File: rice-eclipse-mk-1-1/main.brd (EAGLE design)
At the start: 110.2 x 91.2 mm, 75 parts, among them IC1 LMV321LICTRT, IC2 LMV321LICTRT, IC3 LMV321LICTRT, IC4 LMV321LICTRT, U1 LM1084ISX-5.0/NOPB, U2 THS4531IDRD8-M, U3 THS4531IDRD8-M, U4 THS4531IDRD8-M, U5 THS4531IDRD8-M, U6 1101M2S3CQE2, X1 2540-5

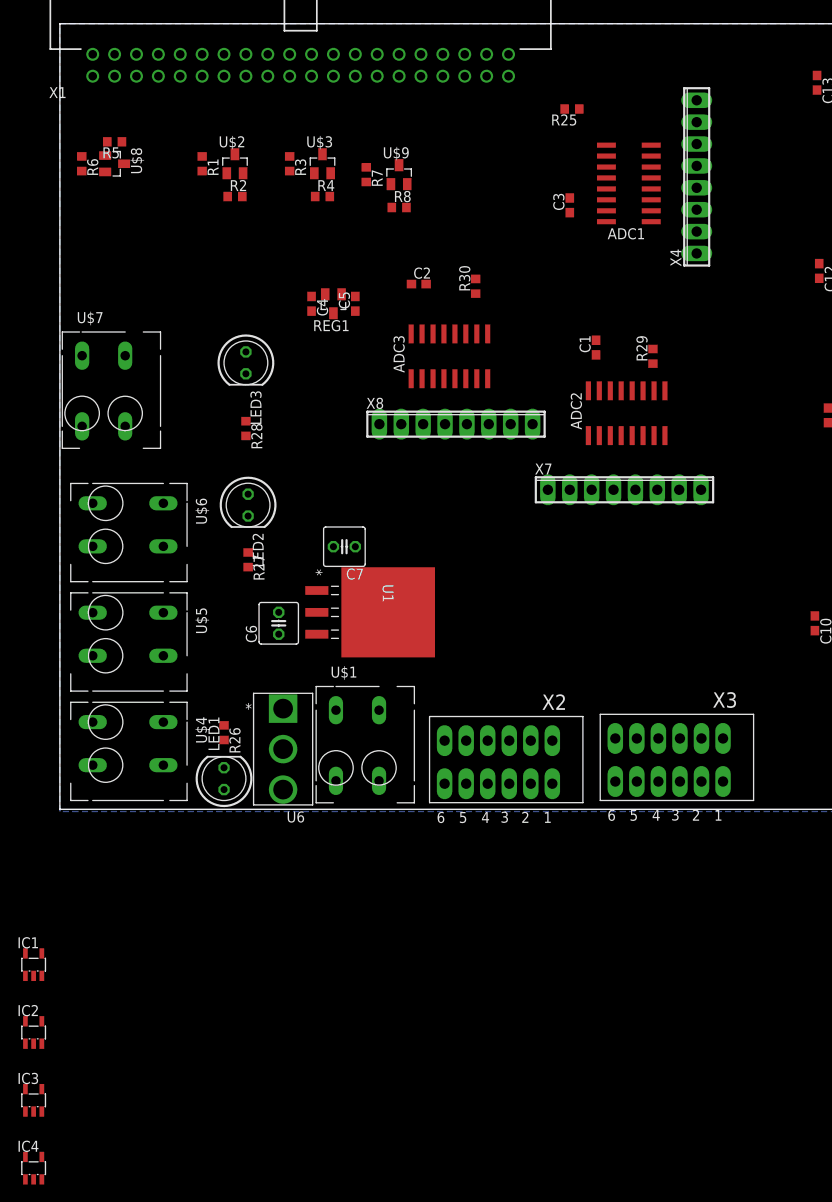
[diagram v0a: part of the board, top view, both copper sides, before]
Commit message: Added initial PT circuit guess and
added some routes for power.
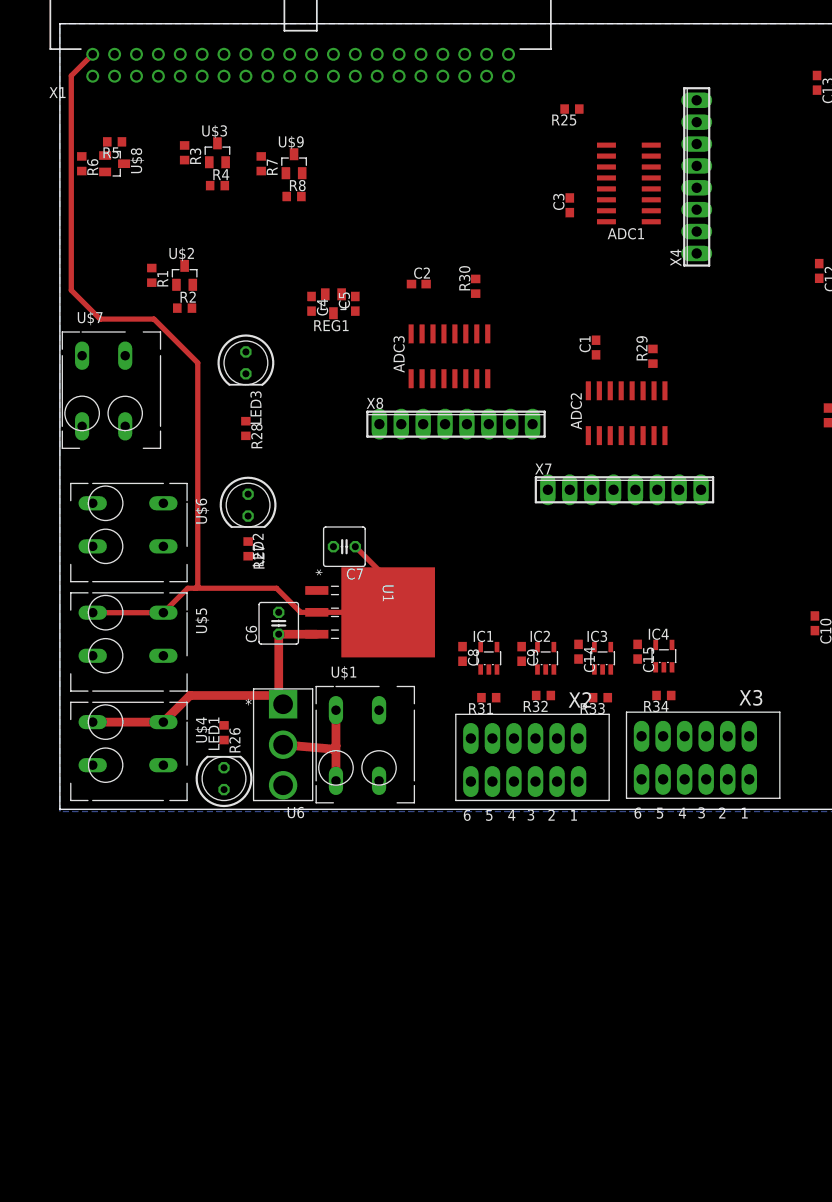
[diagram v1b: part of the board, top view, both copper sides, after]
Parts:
- added C14, C15, C8, C9: 10nF, rcl:C0603
- added R31, R32, R33, R34: 150, rcl:R0603
- moved IC4 94.3 mm to (70.1, 17.8)
- moved IC3 83.6 mm to (63.0, 17.5)
- moved IC2 73.6 mm to (56.4, 17.5)
- moved IC1 63.7 mm to (49.8, 17.5)
- moved R1 14.2 mm to (10.7, 62.0)
- moved R2 14.2 mm to (14.5, 58.2)
- moved U$2 14.2 mm to (14.5, 62.0)
- moved R7 12.3 mm to (23.4, 74.9)
- moved R3 12.3 mm to (14.5, 76.2)
- moved R4 12.3 mm to (18.3, 72.4)
- moved U$3 12.3 mm to (18.3, 76.2)
- moved R8 12.3 mm to (27.2, 71.1)
- moved U$9 12.3 mm to (27.2, 74.9)
- moved X3 3.06 mm to (83.6, 11.2)
- moved X2 3.06 mm to (63.8, 10.9)
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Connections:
- new net PT1_VS-: IC1.1, R31.2, X2.P$11, X2.P$5
- new net PT2_VS-: IC2.1, R32.2, X2.P$3, X2.P$9
- new net PT3_VS-: IC3.1, R33.2, X2.P$1, X2.P$7
- new net PT4_VS-: IC4.1, R34.2, X3.P$11, X3.P$5
- net +12V: now also X2.P$10, X2.P$12, X2.P$2, X2.P$4, X2.P$6, X2.P$8, X3.P$12, X3.P$6
- net +3V3: now also C14.1, C15.1, C8.1, C9.1, IC1.5, IC2.5, IC3.5, IC4.5
- net ADC2_A0: now also IC1.3, IC1.4; no longer X2.P$12, X2.P$6
- net ADC2_A1: now also IC2.3, IC2.4; no longer X2.P$11, X2.P$5
- net ADC2_A2: now also IC3.3, IC3.4; no longer X2.P$10, X2.P$4
- net ADC2_A3: now also IC4.3, IC4.4; no longer X2.P$3, X2.P$9
- net ADC2_A4: now also X3.P$10, X3.P$4
- net ADC2_A5: now also X3.P$3, X3.P$9
- net ADC2_A6: now also X3.P$2, X3.P$8
- net ADC2_A7: now also X3.P$1, X3.P$7
- net GND: now also C14.2, C15.2, C8.2, C9.2, IC1.2, IC2.2, IC3.2, IC4.2, R31.1, R32.1, R33.1, R34.1
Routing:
- net +5V: track 0.00 -> 118.7 mm
- net +12V: track 0.00 -> 35.9 mm
- net +12V_DEBUG: track 0.00 -> 14.5 mm
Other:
- board text added: "TODO: Flyback diode?"

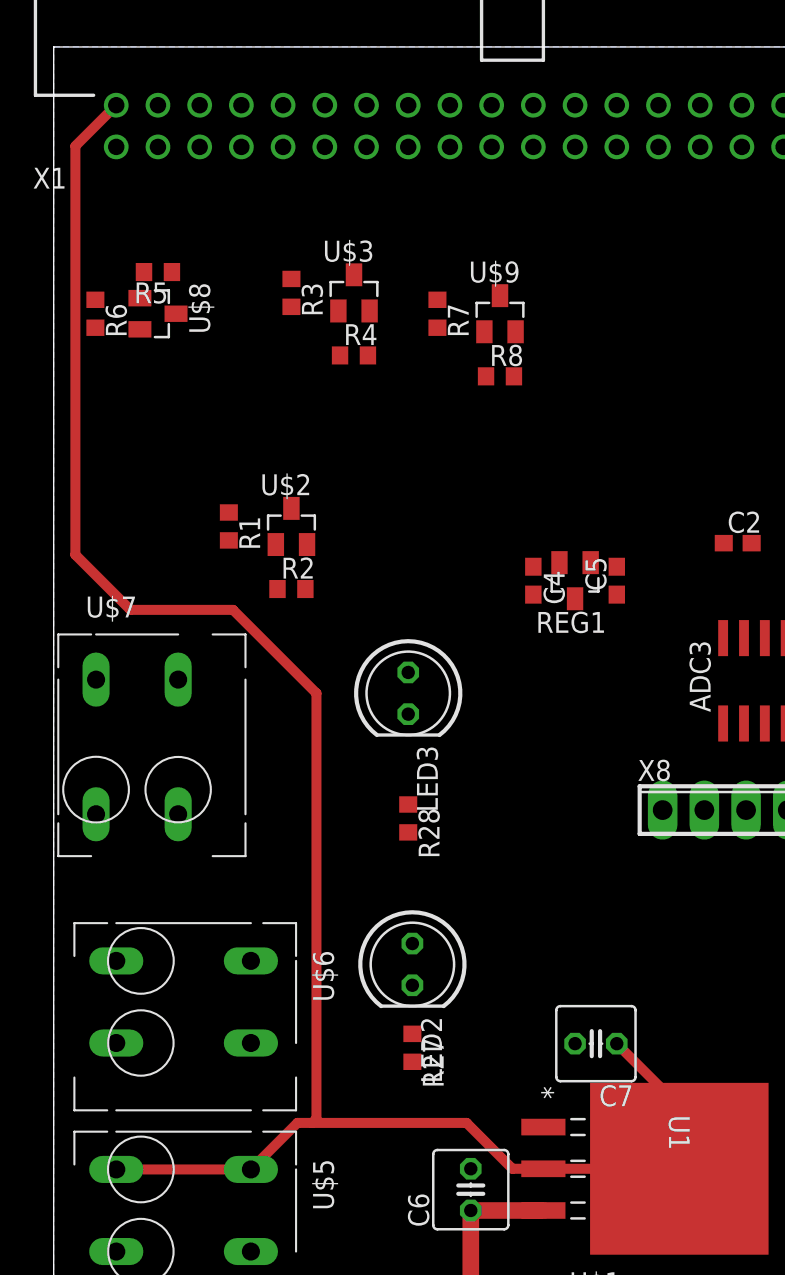
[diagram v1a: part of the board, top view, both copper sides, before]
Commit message: Slightly increased size of power traces.
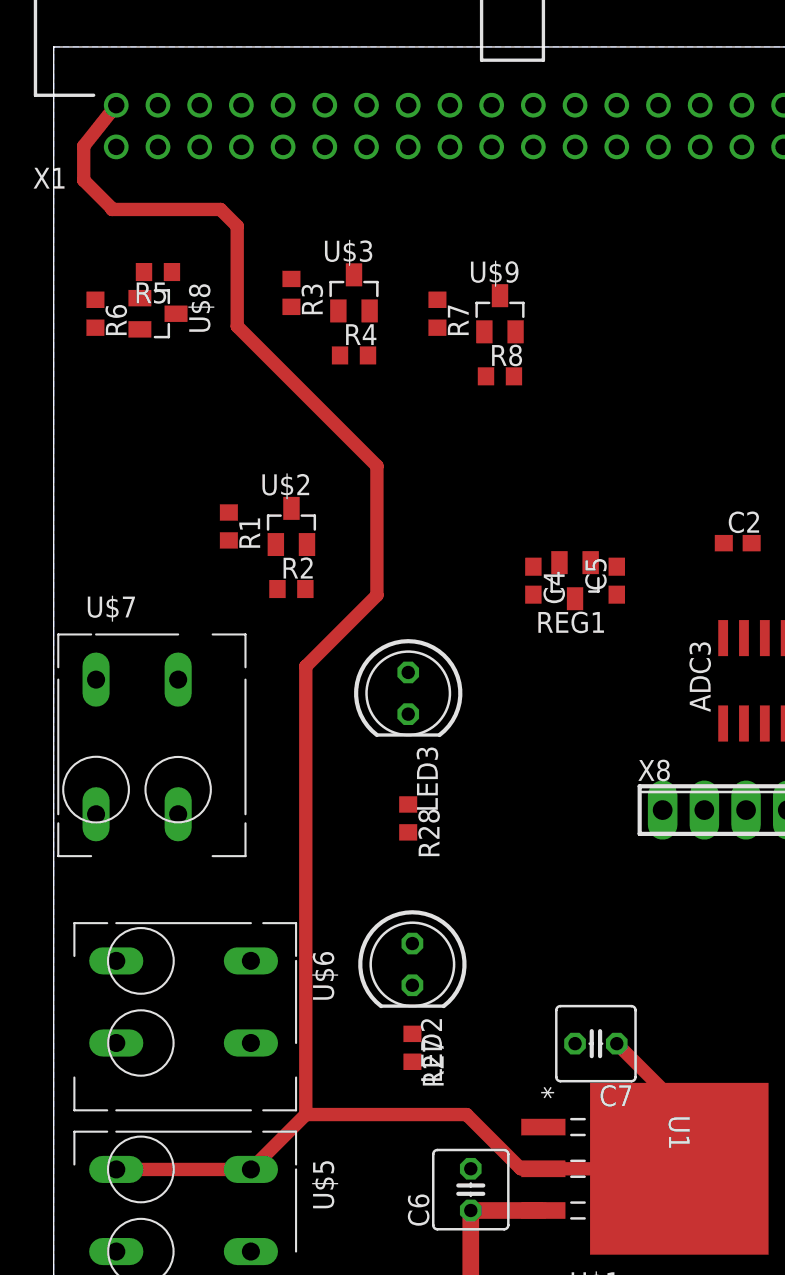
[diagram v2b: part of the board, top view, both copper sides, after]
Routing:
- net +5V: track 118.7 -> 130.6 mm
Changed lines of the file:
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@@
 <contactref element="U1" pad="4"/>
 <contactref element="LED2" pad="A"/>
-<wire x1="12.01" y1="22.82" x2="3.81" y2="22.82" width="0.6096" layer="1"/>
-<wire x1="27.94" y1="22.86" x2="29.8196" y2="22.86" width="0.6096" layer="1"/>
-<wire x1="27.94" y1="22.86" x2="25.146" y2="25.654" width="0.6096" layer="1"/>
-<wire x1="15.748" y1="25.654" x2="25.146" y2="25.654" width="0.6096" layer="1"/>
-<wire x1="15.748" y1="25.654" x2="14.844" y2="25.654" width="0.6096" layer="1"/>
-<wire x1="14.844" y1="25.654" x2="12.01" y2="22.82" width="0.6096" layer="1"/>
-<wire x1="38.1" y1="22.86" x2="29.8196" y2="22.86" width="0.6096" layer="1"/>
-<wire x1="34.29" y1="30.48" x2="38.1" y2="26.67" width="0.6096" layer="1"/>
+<wire x1="38.1" y1="26.67" x2="34.29" y2="30.48" width="0.6096" layer="1"/>
 <wire x1="38.1" y1="26.67" x2="38.1" y2="22.86" width="0.6096" layer="1"/>
-<wire x1="3.81" y1="87.63" x2="1.3208" y2="85.1408" width="0.6096" layer="1"/>
-<wire x1="1.3208" y1="60.2488" x2="4.6736" y2="56.896" width="0.6096" layer="1"/>
-<wire x1="4.6736" y1="56.896" x2="10.922" y2="56.896" width="0.6096" layer="1"/>
-<wire x1="10.922" y1="56.896" x2="16.002" y2="51.816" width="0.6096" layer="1"/>
-<wire x1="16.002" y1="51.816" x2="16.002" y2="41.402" width="0" layer="19" extent="1-16"/>
-<wire x1="16.002" y1="41.402" x2="20.828" y2="36.576" width="0" layer="19" extent="1-16"/>
-<wire x1="20.828" y1="36.576" x2="21.844" y2="36.576" width="0" layer="19" extent="1-16"/>
-<wire x1="1.3208" y1="85.1408" x2="1.3208" y2="60.2488" width="0.6096" layer="1"/>
-<wire x1="16.002" y1="51.816" x2="16.002" y2="25.908" width="0.6096" layer="1"/>
-<wire x1="16.002" y1="25.908" x2="15.748" y2="25.654" width="0.6096" layer="1"/>
+<wire x1="1.8288" y1="85.1408" x2="3.81" y2="87.63" width="0.8128" layer="1"/>
+<wire x1="3.556" y1="81.28" x2="10.16" y2="81.28" width="0.8128" layer="1"/>
+<wire x1="1.8288" y1="85.1408" x2="1.8288" y2="83.058" width="0.8128" layer="1"/>
+<wire x1="11.176" y1="80.264" x2="10.16" y2="81.28" width="0.8128" layer="1"/>
+<wire x1="37.846" y1="22.86" x2="38.1" y2="22.86" width="0.8128" layer="1"/>
+<wire x1="37.846" y1="22.86" x2="29.8196" y2="22.86" width="0.8128" layer="1"/>
+<wire x1="29.8196" y1="22.86" x2="28.448" y2="22.86" width="0.8128" layer="1"/>
+<wire x1="28.448" y1="22.86" x2="25.146" y2="26.162" width="0.8128" layer="1"/>
+<wire x1="25.146" y1="26.162" x2="15.352" y2="26.162" width="0.8128" layer="1"/>
+<wire x1="15.352" y1="26.162" x2="12.01" y2="22.82" width="0.8128" layer="1"/>
+<wire x1="12.01" y1="22.82" x2="3.81" y2="22.82" width="0.8128" layer="1"/>
+<wire x1="15.352" y1="26.162" x2="15.352" y2="53.452" width="0.8128" layer="1"/>
+<wire x1="19.685" y1="57.785" x2="15.352" y2="53.452" width="0.8128" layer="1"/>
+<wire x1="11.176" y1="80.264" x2="11.176" y2="74.168" width="0.8128" layer="1"/>
+<wire x1="11.176" y1="74.168" x2="19.685" y2="65.659" width="0.8128" layer="1"/>
+<wire x1="19.685" y1="65.659" x2="19.685" y2="57.785" width="0.8128" layer="1"/>
+<wire x1="1.8288" y1="83.058" x2="3.556" y2="81.3308" width="0.8128" layer="1"/>
+<wire x1="3.556" y1="81.3308" x2="3.556" y2="81.28" width="0.8128" layer="1"/>
+<wire x1="34.29" y1="30.48" x2="37.846" y2="26.924" width="0.8128" layer="1"/>
+<wire x1="37.846" y1="26.924" x2="37.846" y2="22.86" width="0.8128" layer="1"/>
+<wire x1="25.146" y1="26.162" x2="21.844" y2="36.576" width="0" layer="19" extent="1-1"/>
 </signal>
 <signal name="N$13">

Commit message: Made a bunch of stuff.
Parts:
- added C16: 0.1UF, rcl:E2,5-5
- added C17: 0.33UF, rcl:E2,5-5
- added C18: 10nF, rcl:C0603
- added C19, C20: (no value), rcl:C025-025X050
- added IC5: UA78M, texas-extra:TO220S
- added IC6: LMV321LICTRT, st-microelectronics-extra:SOT23-5
- added JP1, JP2, JP3: (no value), pinhead:1X02
- added LED4: (no value), led:LED5MM
- added R35: 470, resistor:R0603
- added R36, R37, R38, R39, R40, R41: ?, rcl:0204/7
- added U7: 1101M2S3CQE2, SLIDE_SW:1101M2S3CQE2
- C4, C5: device rcl:C0603 -> rcl:E2,5-5
- C6, C7: device rcl:C025-050X050 -> rcl:E2,5-5
- R31: value 150 -> 10
- moved C4 5.68 mm to (31.8, 63.8), turned to 0 degrees
- moved C5 2.03 mm to (36.3, 58.7)
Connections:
- new net +3V3_ADC: ADC1.15, ADC1.16, ADC2.15, ADC2.16, ADC3.15, ADC3.16, C1.1, C2.1, C3.1, JP1.2, R25.2, R29.2, R30.2
- new net +3V3_LC: C10.1, C11.1, C12.1, C13.1, JP3.2, R12.2, R17.2, R21.2, R9.2, U2.3, U3.3, U4.3, U5.3
- new net +3V3_PT: C14.1, C15.1, C18.1, C8.1, C9.1, IC1.5, IC2.5, IC3.5, IC4.5, IC6.5, JP2.2, R38.1
- new net +5V_RPI: X1.2
- new net N$10: IC1.3, R36.1, R37.2
- new net N$11: C19.1, R40.2, R41.1
- new net N$12: IC1.1, R38.2, R39.1
- new net N$25: C20.1, IC6.1, R40.1
- new net N$4: C16.+, IC5.3, U7.2
- new net N$9: LED4.K, R35.1
- new net PT1_PREC: IC1.4, R37.1, R41.2
- net +10V: now also C6.+, R35.2, U1.3, U7.1
- net +12V: now also C17.+, IC5.1; no longer C5.1, C6.1, REG1.3, U1.3
- net +3V3: now also C4.+, JP1.1, JP2.1, JP3.1; no longer ADC1.15, ADC1.16, ADC2.15, ADC2.16, ADC3.15, ADC3.16, C1.1, C10.1, C11.1, C12.1, C13.1, C14.1, C15.1, C2.1, C3.1, C4.1, C8.1, C9.1, IC1.5, IC2.5, IC3.5, IC4.5, R12.2, R17.2, R21.2, R25.2, R29.2, R30.2, R9.2, U2.3, U3.3, U4.3, U5.3
- net +5V: now also C5.+, C7.+, REG1.3; no longer C7.1, X1.2
- net ADC2_A0: now also IC6.3, IC6.4; no longer IC1.3, IC1.4
- net GND: now also C16.-, C17.-, C18.2, C19.2, C20.2, C4.-, C5.-, C6.-, C7.-, IC5.2, IC6.2, LED4.A, R39.2; no longer C4.2, C5.2, C6.2, C7.2
- net PT1_VS-: now also R36.2; no longer IC1.1
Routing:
- net +5V: track 130.6 -> 0.00 mm
- net +12V: track 35.9 -> 0.00 mm
- net +12V_DEBUG: track 14.5 -> 0.00 mm

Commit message: Added flyback diodes and moved stuff onto board.
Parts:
- removed U7: 1101M2S3CQE2, SLIDE_SW:1101M2S3CQE2
- added D1, D2, D3, D4: 1N4004, diode:DO41-10
- moved R40 204.7 mm to (49.8, 32.0), turned to 180 degrees
- moved R39 196.8 mm to (41.4, 21.1), turned to 180 degrees
- moved R41 188.4 mm to (49.8, 29.0)
- moved JP3 187.9 mm to (83.3, 32.3)
- moved R38 182.2 mm to (41.4, 18.3)
- moved R37 180.8 mm to (54.1, 23.1), turned to 270 degrees
- moved C20 163.1 mm to (56.1, 30.2), turned to 270 degrees
- moved JP1 154.1 mm to (36.1, 52.1), turned to 90 degrees
- moved C19 146.7 mm to (42.4, 26.4), turned to 270 degrees
- moved JP2 146.2 mm to (38.9, 26.7), turned to 90 degrees
- moved C18 108.0 mm to (48.8, 37.1), turned to 270 degrees
- moved IC6 97.5 mm to (52.8, 36.8)
- moved C17 92.0 mm to (30.2, 16.8), turned to 180 degrees
- moved C16 86.8 mm to (30.0, 27.4)
- moved LED4 68.9 mm to (20.1, 25.9), turned to 270 degrees
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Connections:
- removed net N$4: C16.+, IC5.3, U7.2
- net +10V: now also C16.+, IC5.3; no longer U7.1
- net +12V: now also D1.C, D2.C, D3.C, D4.C
- net RELAY_NEGATIVE: now also D1.A
- net SOLENOID_1_NEGATIVE: now also D2.A
- net SOLENOID_2_NEGATIVE: now also D3.A
- net SOLENOID_3_NEGATIVE: now also D4.A
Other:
- board text removed: "TODO: Flyback diode?"

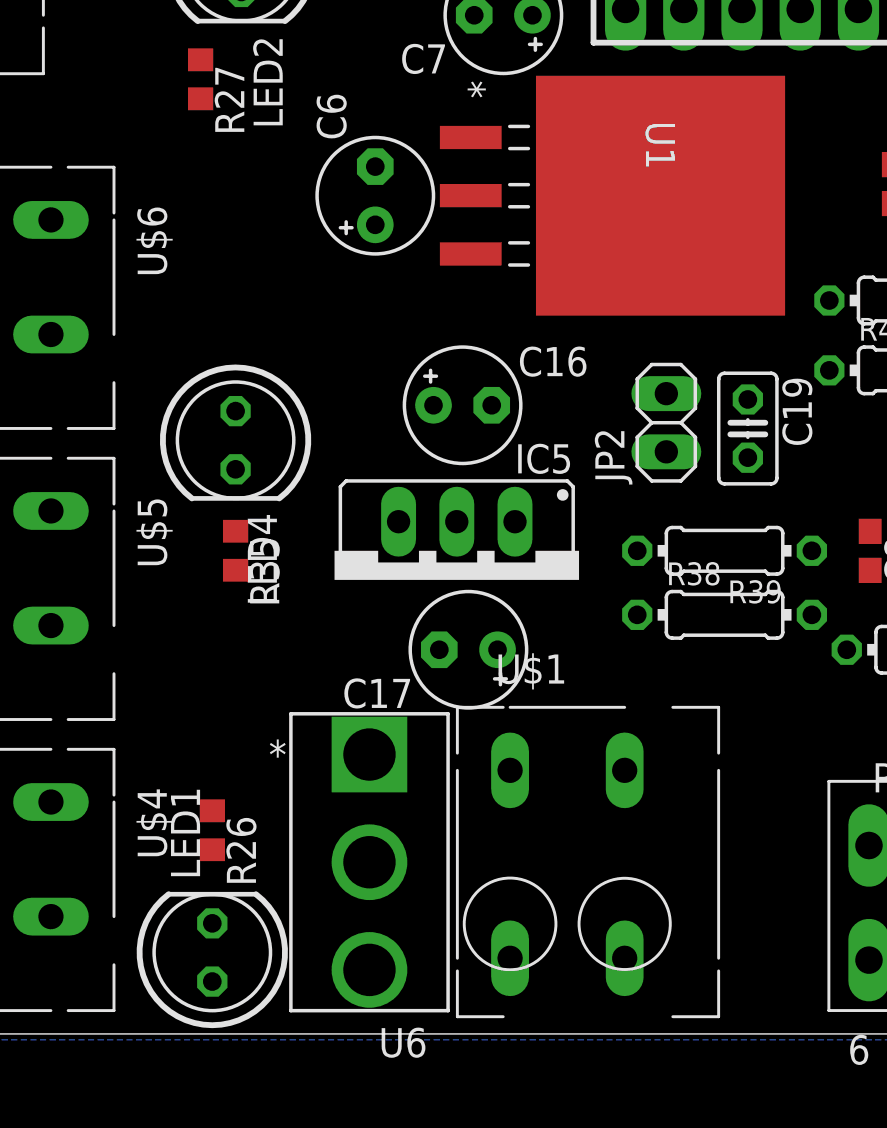
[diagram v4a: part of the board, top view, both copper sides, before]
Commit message: Added schottky diode.
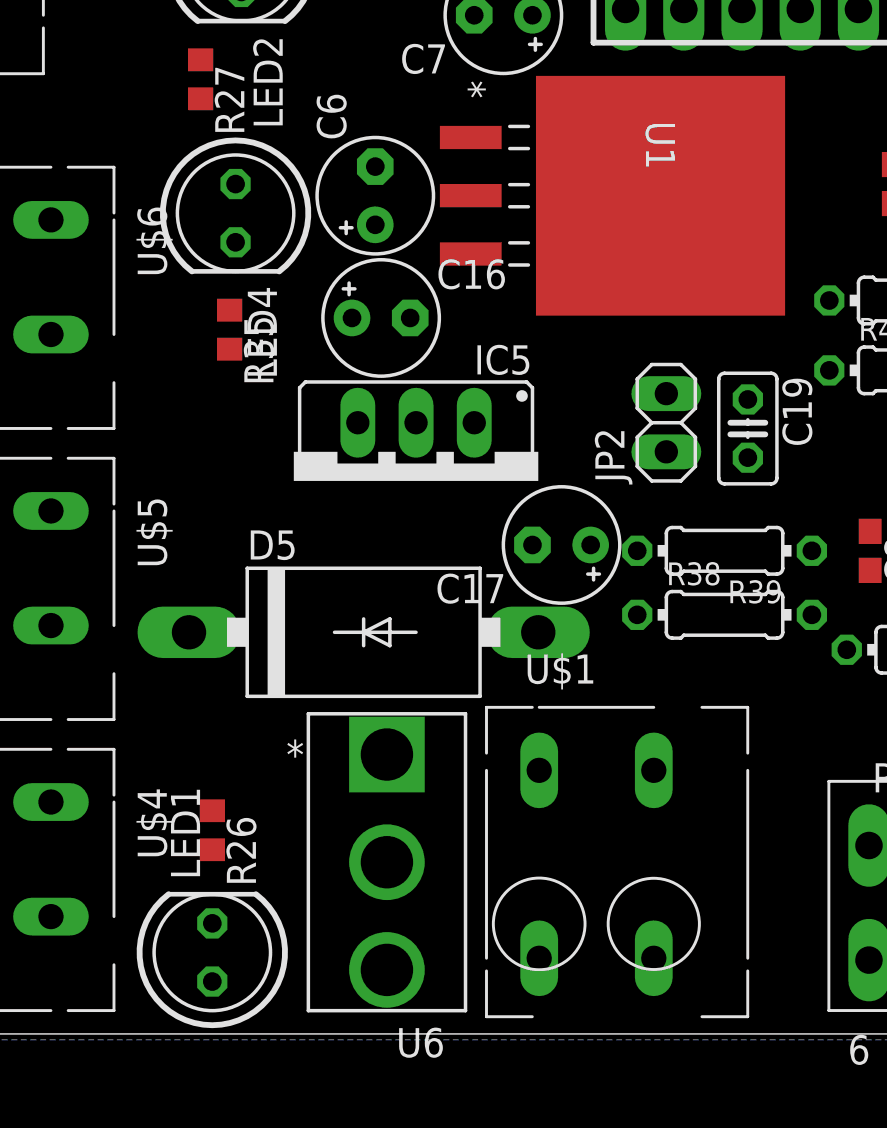
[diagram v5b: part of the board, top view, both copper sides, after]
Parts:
- added D5: (no value), diode:DO201-15
- moved LED4 9.91 mm to (20.1, 35.8)
- moved R35 9.66 mm to (19.8, 30.7)
- moved C17 6.12 mm to (34.3, 21.3)
- moved C16 5.21 mm to (26.4, 31.2)
- moved IC5 4.67 mm to (27.9, 24.1)
- moved U$1 1.27 mm to (35.8, 3.30)
- moved U6 0.76 mm to (26.7, 2.79)
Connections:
- new net N$4: D5.A, U6.1
- net +12V: now also D5.C; no longer U6.1
